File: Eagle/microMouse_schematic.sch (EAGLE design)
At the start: 11 parts, among them IC1 DSPIC33FJ64MC804-PT, IC2 L293D, X1 332-06, X2 332-06, X3 057-006-1, X4 057-006-1

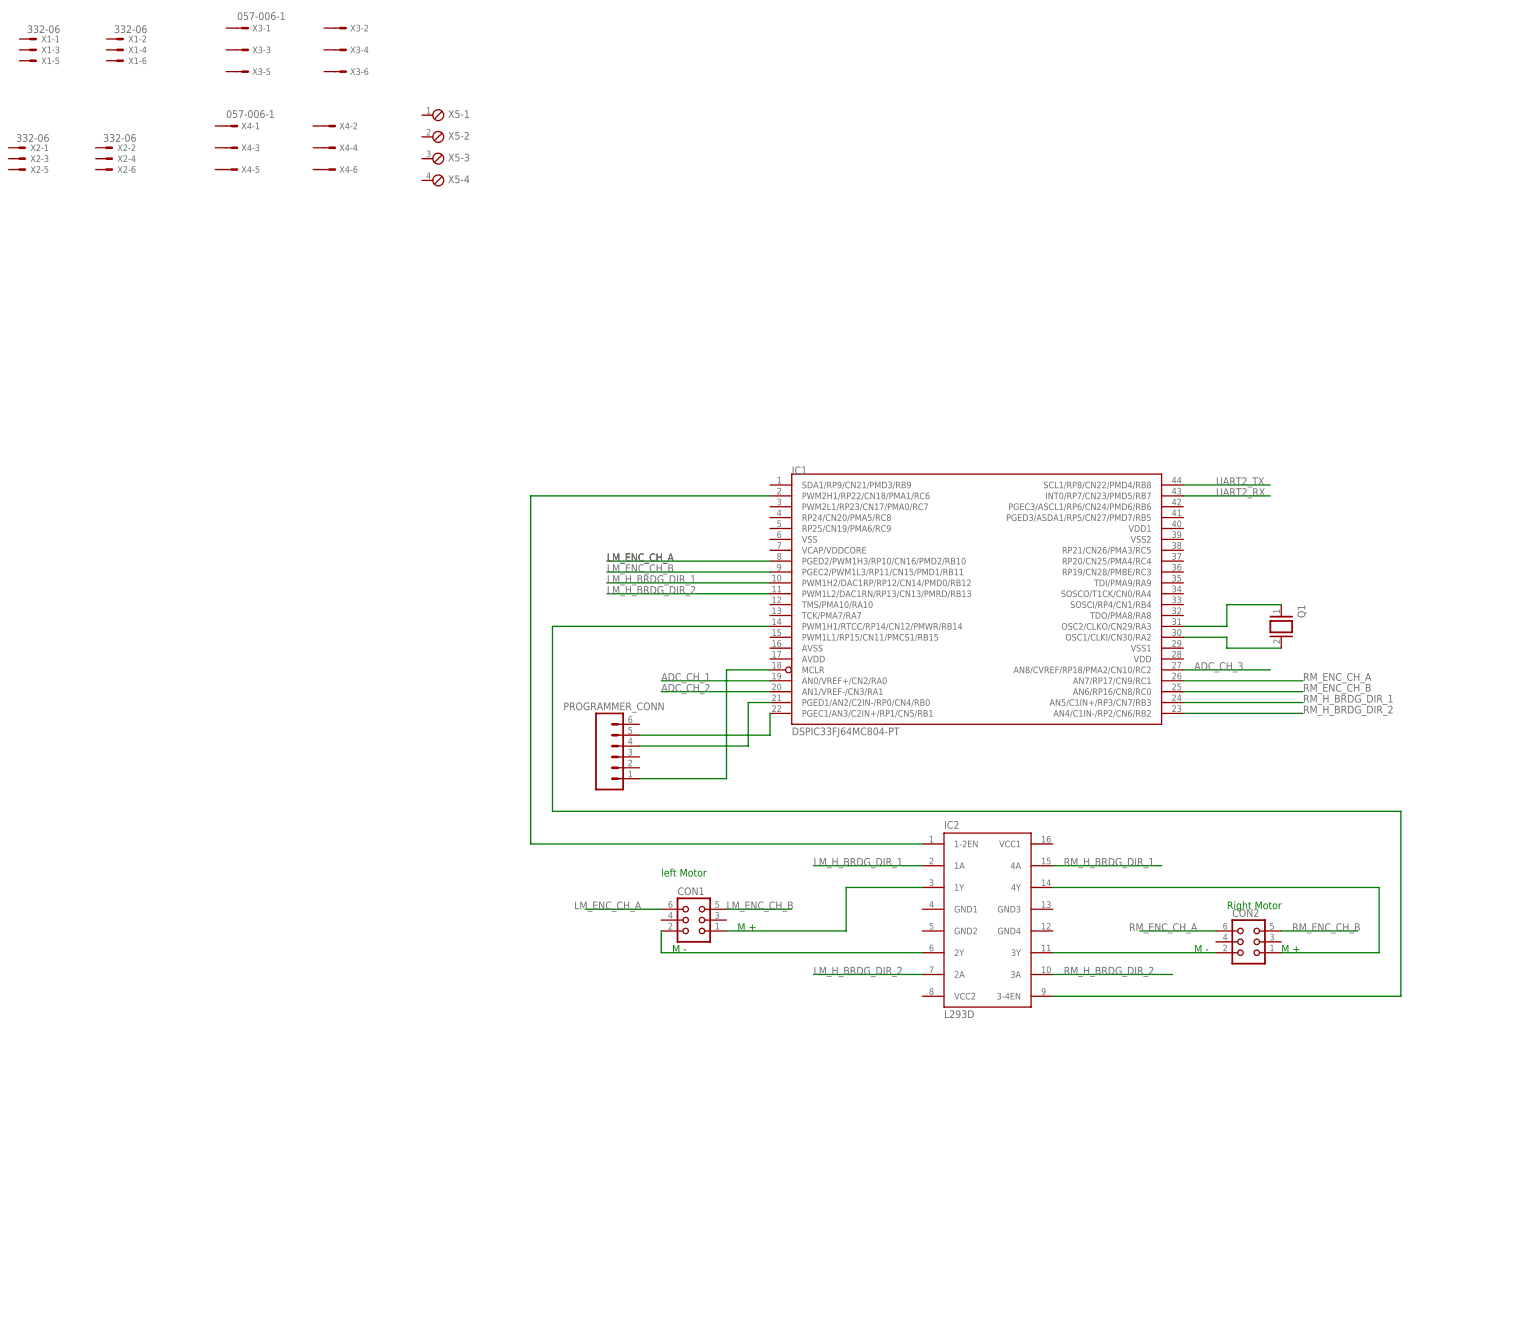
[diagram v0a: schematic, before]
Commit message: [+] added voltage regulator, reset switch, LEDs
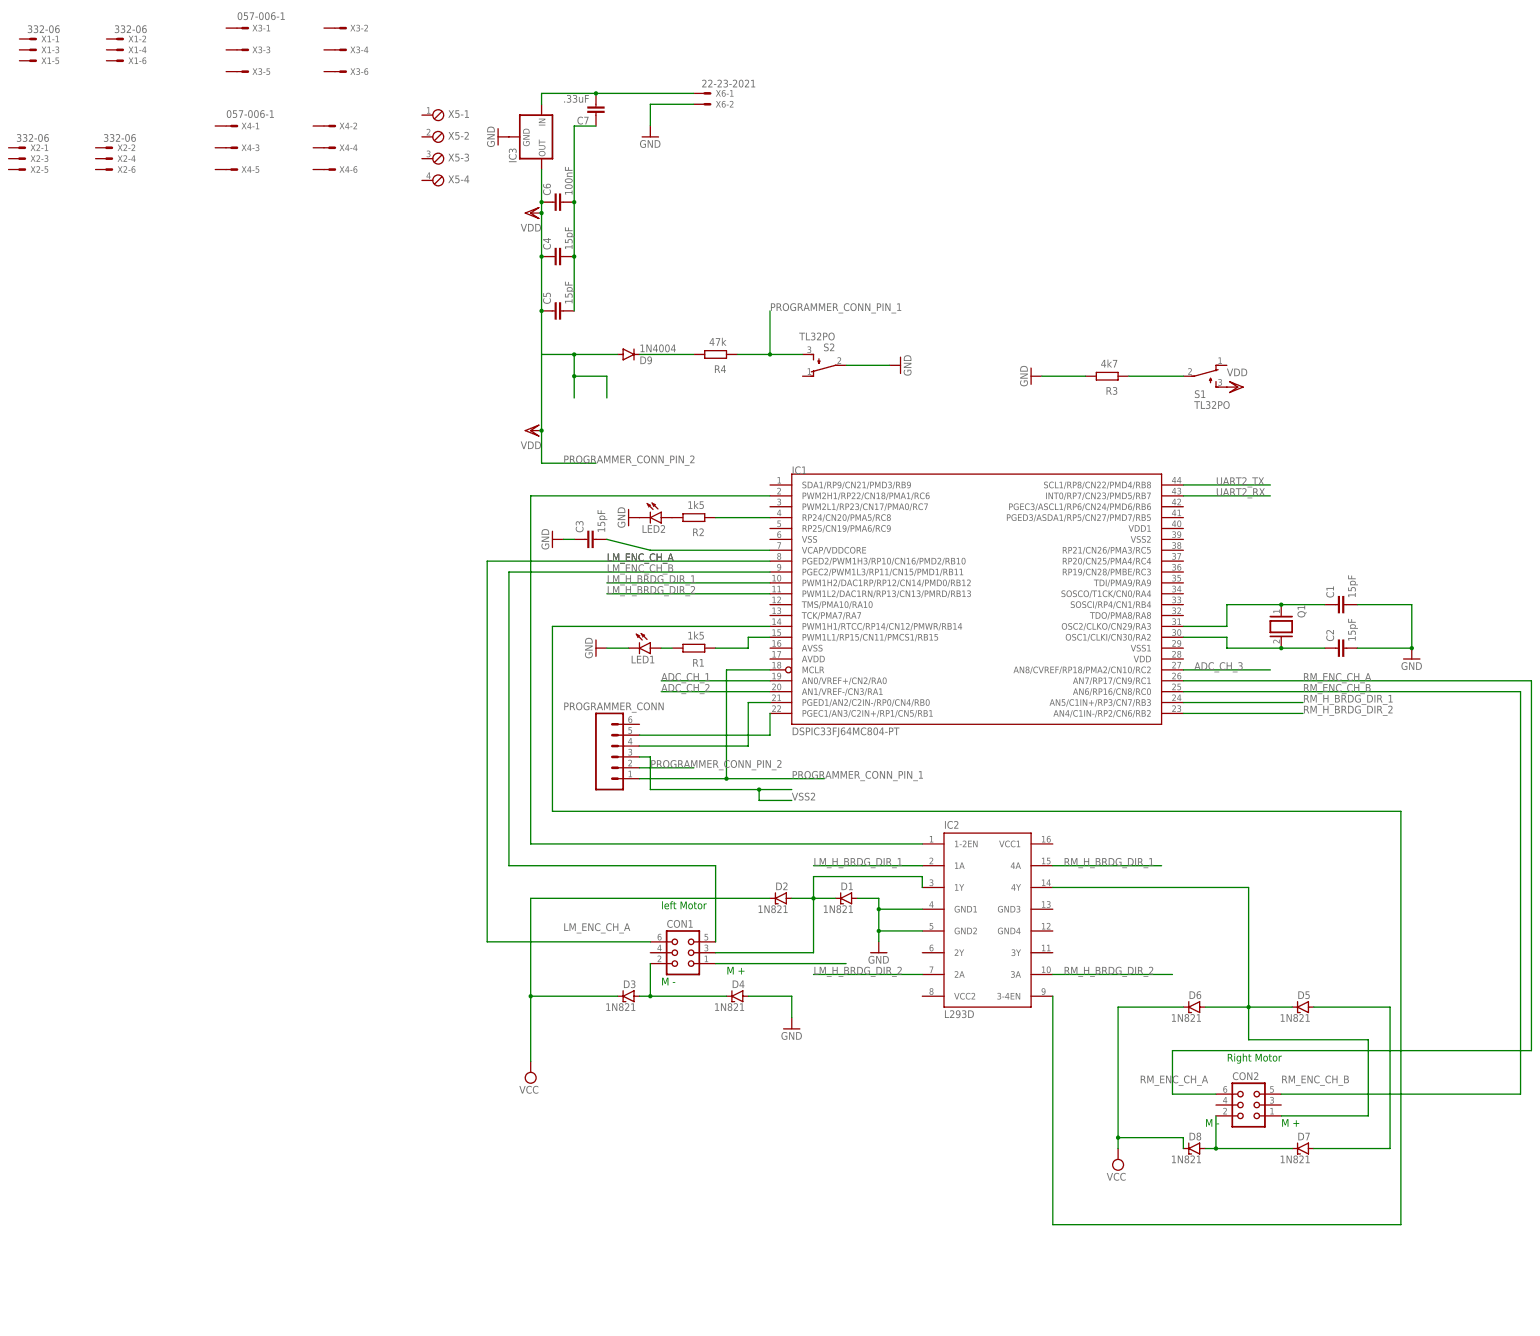
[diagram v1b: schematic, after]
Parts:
- added C1, C2, C3, C4, C5: 15pF, capacitor-wima:C2,5-3
- added C6: 100nF, capacitor-wima:C2,5-3
- added C7: .33uF, capacitor-wima:C2,5-3
- added D1, D2, D3, D4, D5, D6, D7, D8: 1N821, diode:1N821
- added D9: 1N4004, diode:1N4004
- added IC3: (no value), v-reg:78LXX
- added LED1, LED2: (no value), led:LED
- added R1, R2: 1k5, ngspice-simulation:R
- added R3: 4k7, ngspice-simulation:R
- added R4: 47k, ngspice-simulation:R
- added S1, S2: TL32PO, switch:TL32PO
- added X6: 22-23-2021, con-molex:22-23-2021
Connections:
- new net GND: C1.2, C2.2, C3.1, D1.A, D4.A, IC2.GND1, IC2.GND2, IC3.GND, LED1.C, LED2.C, R3.2, S2.P, X6-2.S
- new net N$1: IC1.RP24/CN20/PMA5/RC8, R2.1
- new net N$13: R3.1, S1.P
- new net N$14: IC1.PWM1L1/RP15/CN11/PMCS1/RB15, R1.1
- new net N$16: CON2.2, D7.C, D8.A
- new net N$17: LED1.A, R1.2
- new net N$19: D9.C, R4.2
- new net N$20: D9.A
- new net N$21: C4.2, C5.2, C6.2, C7.1
- new net N$22: C7.2, IC3.IN, X6-1.S
- new net N$4: CON1.3, D1.C, D2.A, IC2.1Y
- new net PROGRAMMER_CONN_PIN_1: IC1.MCLR, PROGRAMMER_CONN.1, R4.1, S2.S
- new net PROGRAMMER_CONN_PIN_2: C4.1, C5.1, C6.1, IC3.OUT, PROGRAMMER_CONN.2
- new net VCAP/VDDCORE: C3.2, IC1.VCAP/VDDCORE
- new net VCC: D2.C, D3.C, D6.C, D8.C
- new net VDD: S1.S
- new net VSS2: PROGRAMMER_CONN.3
- net N$10: now also C2.1
- net N$11: now also C1.1
- net N$3: now also LED2.A, R2.2; no longer IC1.MCLR, PROGRAMMER_CONN.1
- net N$6: no longer IC2.1Y
- net N$7: now also D3.A, D4.C; no longer IC2.2Y
- net N$8: now also D5.C, D6.A
- net N$9: now also D5.A, D7.A; no longer CON2.2, IC2.3Y
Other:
- moved on the sheet: CON1, CON2

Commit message: [~] clean up unused wire and component
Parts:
- removed R3: 4k7, ngspice-simulation:R
- removed S1: TL32PO, switch:TL32PO
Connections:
- net N$15 renamed PWM_1_RIGHT_MOTOR
- net N$2 renamed PWM_2_LEFT_MOTOR
- net N$20 renamed AVDD
- removed net N$13: R3.1, S1.P
- removed net VDD: S1.S
- new net N$2: CON2.5
- net GND: no longer R3.2
- net RM_ENC_CH_B: no longer CON2.5
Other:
- note added: "AVDD"
- note added: "VDD"
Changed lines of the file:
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@@
 <part name="C2" library="capacitor-wima" library_urn="urn:adsk.eagle:library:116" deviceset="C" device="2,5-3" package3d_urn="urn:adsk.eagle:package:5436/1" value="15pF"/>
 <part name="GND3" library="supply1" library_urn="urn:adsk.eagle:library:371" deviceset="GND" device=""/>
-<part name="R3" library="ngspice-simulation" library_urn="urn:adsk.eagle:library:527439" deviceset="R" device="" value="4k7"/>
-<part name="S1" library="switch" library_urn="urn:adsk.eagle:library:380" deviceset="TL32PO" device="" package3d_urn="urn:adsk.eagle:package:27745/1"/>
-<part name="GND4" library="supply1" library_urn="urn:adsk.eagle:library:371" deviceset="GND" device=""/>
-<part name="VDD1" library="supply1" library_urn="urn:adsk.eagle:library:371" deviceset="VDD" device=""/>
 <part name="R1" library="ngspice-simulation" library_urn="urn:adsk.eagle:library:527439" deviceset="R" device="" value="1k5"/>
 <part name="LED1" library="led" library_urn="urn:adsk.eagle:library:259" deviceset="LED" device="" package3d_urn="urn:adsk.eagle:package:15825/1"/>
@@
 <text x="-152.4" y="43.18" size="1.778" layer="91">M -</text>
 <text x="-25.4" y="10.16" size="1.778" layer="91">M -</text>
+<text x="-165.1" y="177.8" size="1.778" layer="95">VDD</text>
+<text x="-175.26" y="177.8" size="1.778" layer="95">AVDD</text>
 </plain>
 <instances>
@@
 <attribute name="VALUE" x="20.32" y="116.84" size="1.778" layer="96"/>
 </instance>
-<instance part="R3" gate="G$1" x="-48.26" y="185.42" smashed="yes" rot="R180">
-<attribute name="NAME" x="-45.72" y="182.88" size="1.778" layer="95" rot="R180"/>
-<attribute name="VALUE" x="-45.72" y="189.23" size="1.778" layer="96" rot="R180"/>
-</instance>
-<instance part="S1" gate="BEF1" x="-25.4" y="185.42" smashed="yes" rot="R270">
-<attribute name="NAME" x="-27.94" y="180.34" size="1.778" layer="95"/>
-<attribute name="VALUE" x="-27.94" y="177.8" size="1.778" layer="96"/>
-</instance>
-<instance part="GND4" gate="1" x="-66.04" y="185.42" smashed="yes" rot="R270">
-<attribute name="VALUE" x="-68.58" y="187.96" size="1.778" layer="96" rot="R270"/>
-</instance>
-<instance part="VDD1" gate="G$1" x="-17.78" y="182.88" smashed="yes" rot="R270">
-<attribute name="VALUE" x="-20.32" y="185.42" size="1.778" layer="96"/>
-</instance>
 <instance part="R1" gate="G$1" x="-144.78" y="121.92" smashed="yes" rot="R180">
 <attribute name="NAME" x="-142.24" y="119.38" size="1.778" layer="95" rot="R180"/>
@@
 </busses>
 <nets>
-<net name="N$2" class="0">
-<segment>
-<wire x1="-91.44" y1="76.2" x2="-182.88" y2="76.2" width="0.1524" layer="91"/>
-<pinref part="IC1" gate="G$1" pin="PWM2H1/RP22/CN18/PMA1/RC6"/>
-<wire x1="-182.88" y1="76.2" x2="-182.88" y2="157.48" width="0.1524" layer="91"/>
-<wire x1="-182.88" y1="157.48" x2="-127" y2="157.48" width="0.1524" layer="91"/>
-<pinref part="IC2" gate="G$1" pin="1-2EN"/>
-</segment>
-</net>
 <net name="ADC_CH_1" class="0">
 <segment>
@@
 <segment>
 <pinref part="CON1" gate="G$1" pin="6"/>
-<wire x1="-154.94" y1="53.34" x2="-193.04" y2="53.34" width="0.1524" layer="91"/>
-<label x="-175.26" y="55.88" size="1.778" layer="95"/>
+<wire x1="-154.94" y1="53.34" x2="-172.72" y2="53.34" width="0.1524" layer="91"/>
+<label x="-175.26" y="53.34" size="1.778" layer="95"/>
+</segment>
+<segment>
 <pinref part="IC1" gate="G$1" pin="PGED2/PWM1H3/RP10/CN16/PMD2/RB10"/>
-<wire x1="-127" y1="142.24" x2="-193.04" y2="142.24" width="0.1524" layer="91"/>
+<wire x1="-127" y1="142.24" x2="-165.1" y2="142.24" width="0.1524" layer="91"/>
 <label x="-165.1" y="142.24" size="1.778" layer="95"/>
-<label x="-165.1" y="142.24" size="1.778" layer="95"/>
-<wire x1="-193.04" y1="53.34" x2="-193.04" y2="142.24" width="0.1524" layer="91"/>
 </segment>
 </net>
 <net name="LM_ENC_CH_B" class="0">
 <segment>
+<pinref part="CON1" gate="G$1" pin="5"/>
+<wire x1="-139.7" y1="53.34" x2="-124.46" y2="53.34" width="0.1524" layer="91"/>
+<label x="-139.7" y="53.34" size="1.778" layer="95"/>
+</segment>
+<segment>
 <pinref part="IC1" gate="G$1" pin="PGEC2/PWM1L3/RP11/CN15/PMD1/RB11"/>
-<wire x1="-127" y1="139.7" x2="-187.96" y2="139.7" width="0.1524" layer="91"/>
+<wire x1="-127" y1="139.7" x2="-165.1" y2="139.7" width="0.1524" layer="91"/>
 <label x="-165.1" y="139.7" size="1.778" layer="95"/>
-<pinref part="CON1" gate="G$1" pin="5"/>
-<wire x1="-139.7" y1="53.34" x2="-139.7" y2="71.12" width="0.1524" layer="91"/>
-<wire x1="-139.7" y1="71.12" x2="-187.96" y2="71.12" width="0.1524" layer="91"/>
-<wire x1="-187.96" y1="71.12" x2="-187.96" y2="139.7" width="0.1524" layer="91"/>
 </segment>
 </net>
@@
 <wire x1="-22.86" y1="17.78" x2="-33.02" y2="17.78" width="0.1524" layer="91"/>
 <label x="-40.64" y="20.32" size="1.778" layer="95"/>
-<wire x1="-33.02" y1="17.78" x2="-33.02" y2="27.94" width="0.1524" layer="91"/>
-<wire x1="-33.02" y1="27.94" x2="50.8" y2="27.94" width="0.1524" layer="91"/>
-<label x="-2.54" y="114.3" size="1.778" layer="95"/>
+</segment>
+<segment>
 <pinref part="IC1" gate="G$1" pin="AN7/RP17/CN9/RC1"/>
-<wire x1="50.8" y1="27.94" x2="50.8" y2="114.3" width="0.1524" layer="91"/>
-<wire x1="50.8" y1="114.3" x2="-30.48" y2="114.3" width="0.1524" layer="91"/>
-</segment>
-</net>
-<net name="RM_ENC_CH_B" class="0">
-<segment>
-<label x="-2.54" y="111.76" size="1.778" layer="95"/>
-<pinref part="IC1" gate="G$1" pin="AN6/RP16/CN8/RC0"/>
-<wire x1="48.26" y1="111.76" x2="-30.48" y2="111.76" width="0.1524" layer="91"/>
-<wire x1="48.26" y1="111.76" x2="48.26" y2="17.78" width="0.1524" layer="91"/>
-<pinref part="CON2" gate="G$1" pin="5"/>
-<label x="-7.62" y="20.32" size="1.778" layer="95"/>
-<wire x1="-7.62" y1="17.78" x2="48.26" y2="17.78" width="0.1524" layer="91"/>
+<wire x1="-30.48" y1="114.3" x2="-10.16" y2="114.3" width="0.1524" layer="91"/>
+<label x="-27.94" y="114.3" size="1.778" layer="95"/>
 </segment>
 </net>
@@
 <pinref part="GND3" gate="1" pin="GND"/>
 <junction x="22.86" y="121.92"/>
-</segment>
-<segment>
-<pinref part="R3" gate="G$1" pin="2"/>
-<wire x1="-53.34" y1="185.42" x2="-63.5" y2="185.42" width="0.1524" layer="91"/>
-<pinref part="GND4" gate="1" pin="GND"/>
 </segment>
 <segment>
@@
 </segment>
 </net>
-<net name="N$15" class="0">
-<segment>
-<pinref part="IC2" gate="G$1" pin="3-4EN"/>
-<wire x1="-60.96" y1="40.64" x2="-60.96" y2="-12.7" width="0.1524" layer="91"/>
-<wire x1="-177.8" y1="83.82" x2="-177.8" y2="127" width="0.1524" layer="91"/>
-<pinref part="IC1" gate="G$1" pin="PWM1H1/RTCC/RP14/CN12/PMWR/RB14"/>
-<wire x1="-177.8" y1="127" x2="-127" y2="127" width="0.1524" layer="91"/>
-<wire x1="-177.8" y1="83.82" x2="20.32" y2="83.82" width="0.1524" layer="91"/>
-<wire x1="20.32" y1="83.82" x2="20.32" y2="-12.7" width="0.1524" layer="91"/>
-<wire x1="-60.96" y1="-12.7" x2="20.32" y2="-12.7" width="0.1524" layer="91"/>
-</segment>
-</net>
 <net name="N$9" class="0">
 <segment>
@@
 </segment>
 </net>
-<net name="N$13" class="0">
-<segment>
-<pinref part="R3" gate="G$1" pin="1"/>
-<pinref part="S1" gate="BEF1" pin="P"/>
-<wire x1="-43.18" y1="185.42" x2="-30.48" y2="185.42" width="0.1524" layer="91"/>
-</segment>
-</net>
-<net name="VDD" class="0">
-<segment>
-<pinref part="S1" gate="BEF1" pin="S"/>
-<pinref part="VDD1" gate="G$1" pin="VDD"/>
-</segment>
-</net>
 <net name="N$17" class="0">
 <segment>
@@
 </segment>
 </net>
-<net name="N$20" class="0">
+<net name="AVDD" class="0">
 <segment>
 <pinref part="D9" gate="1" pin="A"/>
 <wire x1="-162.56" y1="190.5" x2="-172.72" y2="190.5" width="0.1524" layer="91"/>
 <wire x1="-172.72" y1="190.5" x2="-180.34" y2="190.5" width="0.1524" layer="91"/>
+<junction x="-172.72" y="190.5"/>
 <wire x1="-172.72" y1="180.34" x2="-172.72" y2="185.42" width="0.1524" layer="91"/>
-<junction x="-172.72" y="190.5"/>
 <wire x1="-172.72" y1="185.42" x2="-172.72" y2="190.5" width="0.1524" layer="91"/>
 <wire x1="-165.1" y1="180.34" x2="-165.1" y2="185.42" width="0.1524" layer="91"/>
-<wire x1="-165.1" y1="185.42" x2="-172.72" y2="185.42" width="0.1524" layer="91"/>
+<wire x1="-172.72" y1="185.42" x2="-165.1" y2="185.42" width="0.1524" layer="91"/>
 <junction x="-172.72" y="185.42"/>
 </segment>
@@
 </segment>
 </net>
+<net name="PWM_2_LEFT_MOTOR" class="0">
+<segment>
+<pinref part="IC1" gate="G$1" pin="PWM2H1/RP22/CN18/PMA1/RC6"/>
+<wire x1="-127" y1="157.48" x2="-165.1" y2="157.48" width="0.1524" layer="91"/>
+<label x="-165.1" y="157.48" size="1.778" layer="95"/>
+</segment>
+<segment>
+<pinref part="IC2" gate="G$1" pin="1-2EN"/>
+<wire x1="-91.44" y1="76.2" x2="-116.84" y2="76.2" width="0.1524" layer="91"/>
+<label x="-119.38" y="76.2" size="1.778" layer="95"/>
+</segment>
+</net>
+<net name="PWM_1_RIGHT_MOTOR" class="0">
+<segment>
+<pinref part="IC1" gate="G$1" pin="PWM1H1/RTCC/RP14/CN12/PMWR/RB14"/>
+<wire x1="-127" y1="127" x2="-165.1" y2="127" width="0.1524" layer="91"/>
+<label x="-165.1" y="127" size="1.778" layer="95"/>
+</segment>
+<segment>
+<pinref part="IC2" gate="G$1" pin="3-4EN"/>
+<wire x1="-60.96" y1="40.64" x2="-33.02" y2="40.64" width="0.1524" layer="91"/>
+<label x="-58.42" y="40.64" size="1.778" layer="95"/>
+</segment>
+</net>
+<net name="N$2" class="0">
+<segment>
+<pinref part="CON2" gate="G$1" pin="5"/>
+<wire x1="-7.62" y1="17.78" x2="5.08" y2="17.78" width="0.1524" layer="91"/>
+</segment>
+</net>
+<net name="RM_ENC_CH_B" class="0">
+<segment>
+<pinref part="IC1" gate="G$1" pin="AN6/RP16/CN8/RC0"/>
+<wire x1="-30.48" y1="111.76" x2="-10.16" y2="111.76" width="0.1524" layer="91"/>
+<label x="-27.94" y="111.76" size="1.778" layer="95"/>
+</segment>
+</net>
